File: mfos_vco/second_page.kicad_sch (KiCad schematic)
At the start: 0 parts

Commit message: Firs stages of second page
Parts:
- added C1, C2: 0.1uf, symbol Device:C_Polarized_Small_US
- added C14: 0.002uf, symbol Device:C_Polarized_Small_US
- added D2, D3: 1n4118, symbol Device:D_Small_Filled
- added R1, R6: 100k, symbol Device:R_Small_US
- added R12, R13, R25, R32: 10k, symbol Device:R_Small_US
- added R14, R21: 20K, symbol Device:R_Small_US
- added R20: 47k, symbol Device:R_Small_US
- added R22, R26: 1K, symbol Device:R_Small_US
- added R5, R7: 10k, symbol Device:R_Potentiometer_US
- added U4: TL074, symbol Amplifier_Operational:TL074
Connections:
- new net: R25.1, R32.1, U4.6 (-)
- new net: D3.2 (A), R26.1, R32.2, U4.7
- new net: R12.2, R20.1, U4.2 (-)
- new net: R5.3, R6.1
- new net: D2.2 (A), R20.2, R25.2, U4.1
- new net: C14.1, D2.1 (K), D3.1 (K), R13.1, R21.1
- new net: C1.1, R5.2, U4.3 (+)
- new net: C2.1, R7.2, U4.10 (+)
- new net: R1.1, R7.3
- new net: R14.2, R22.1, U4.8
- new net: R13.2, R14.1, U4.9 (-)
- new net: U4.13 (-), U4.14
- new net +12V: R1.2, R6.2
- new net -12V: C14.2, R21.2
- new net GND: C1.2, C2.2, R5.1, R7.1, U4.12 (+), U4.5 (+)
- new net RAW: R12.1
- new net RMP: R26.2
- new net TRI: R22.2

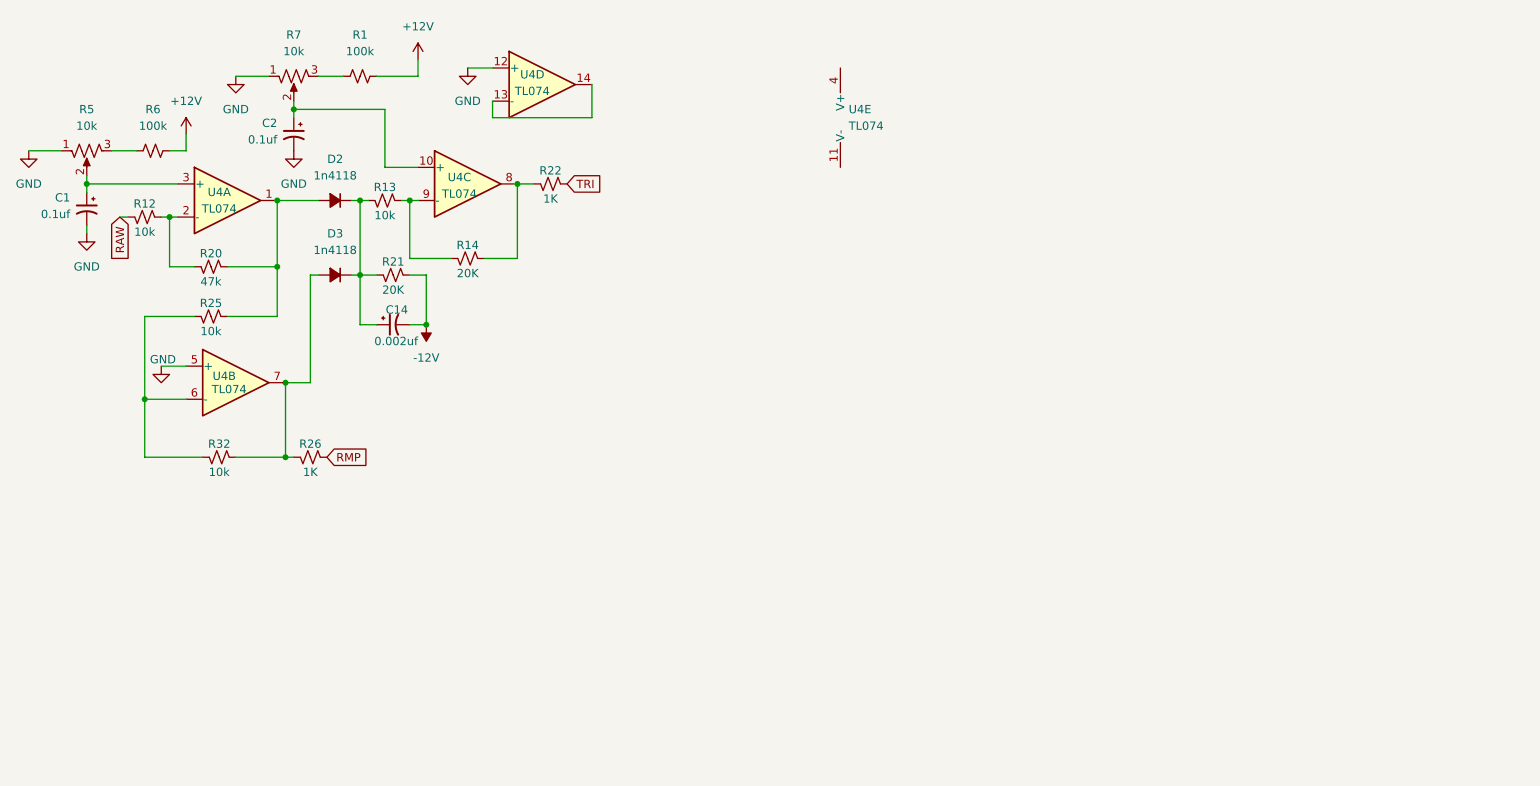
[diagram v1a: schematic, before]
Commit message: finished second page of schematic
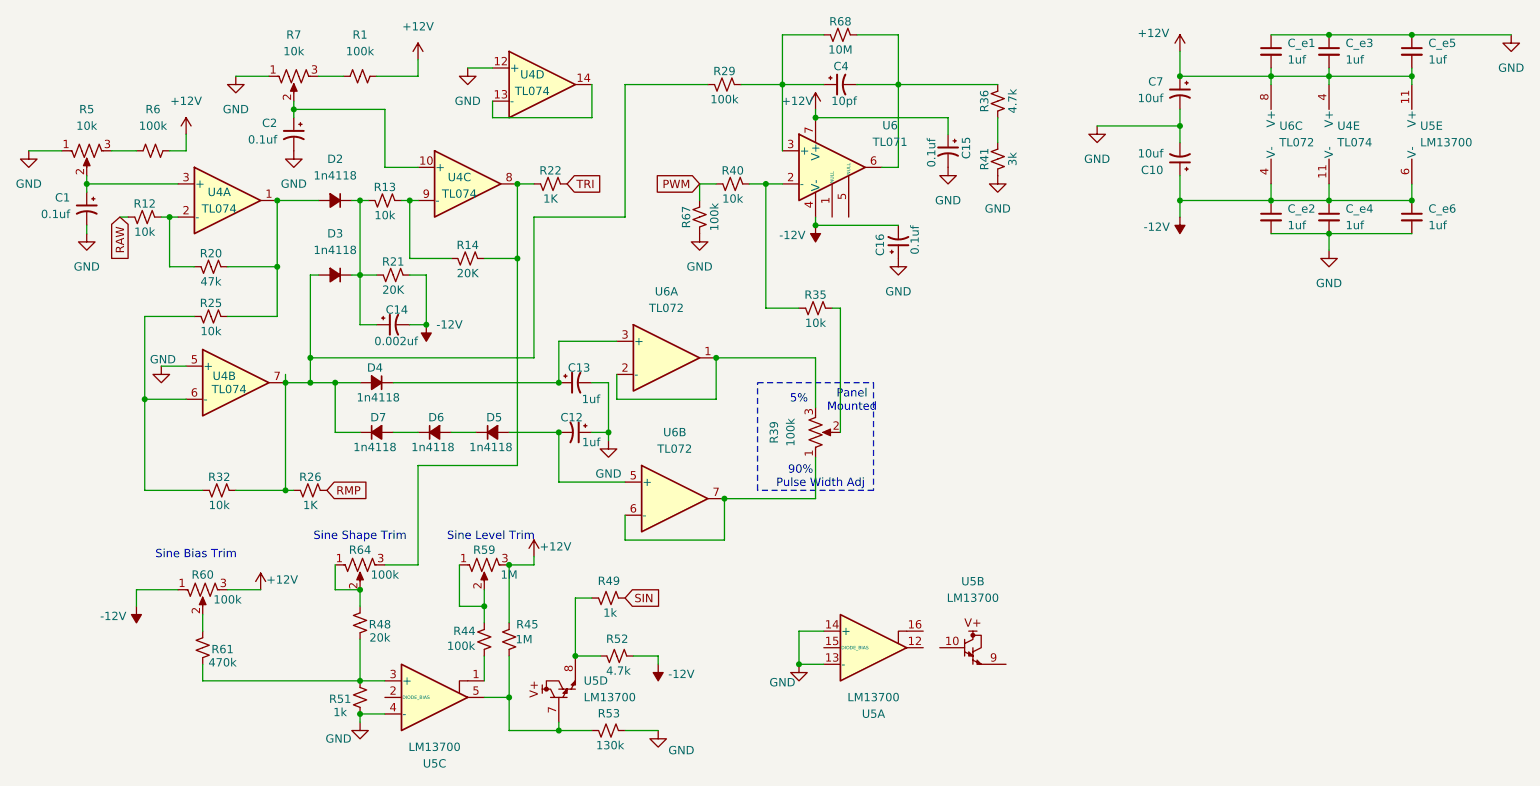
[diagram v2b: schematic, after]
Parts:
- added C10, C7: 10uf, symbol Device:C_Polarized_Small_US
- added C12, C13: 1uf, symbol Device:C_Polarized_Small_US
- added C15, C16: 0.1uf, symbol Device:C_Polarized_Small_US
- added C4: 10pf, symbol Device:C_Polarized_Small_US
- added C_e1, C_e2, C_e3, C_e4, C_e5, C_e6: 1uf, Capacitor_SMD:C_0805_2012Metric_Pad1.18x1.45mm_HandSolder, symbol Device:C_Small
- added D4, D5, D6, D7: 1n4118, symbol Device:D_Small_Filled
- added R29, R44, R67: 100k, symbol Device:R_Small_US
- added R35, R40: 10k, symbol Device:R_Small_US
- added R36, R52: 4.7k, symbol Device:R_Small_US
- added R39, R60, R64: 100k, symbol Device:R_Potentiometer_US
- added R41: 3k, symbol Device:R_Small_US
- added R45: 1M, symbol Device:R_Small_US
- added R48: 20k, symbol Device:R_Small_US
- added R49, R51: 1k, symbol Device:R_Small_US
- added R53: 130k, symbol Device:R_Small_US
- added R59: 1M, symbol Device:R_Potentiometer_US
- added R61: 470k, symbol Device:R_Small_US
- added R68: 10M, symbol Device:R_Small_US
- added U5: LM13700, symbol Amplifier_Operational:LM13700
- added U6: TL072, symbol Amplifier_Operational:TL072
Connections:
- net +12V: now also U4.4 (V+), C15.1, C7.1, C_e1.2, C_e3.2, C_e5.2, R45.2, R59.3, R60.3, U5.11 (V+), U6.7 (V+), U6.8 (V+)
- net -12V: now also U4.11 (V-), C10.1, C16.2, C_e2.1, C_e4.1, C_e6.1, R52.1, R60.1, U5.6 (V-), U6.4 (V-), U6.4 (V-)
- net GND: now also C10.2, C12.1, C13.2, C15.2, C16.1, C7.2, C_e1.1, C_e2.2, C_e3.1, C_e4.2, C_e5.1, C_e6.2, R41.1, R51.1, R53.1, R67.1, U5.13 (-), U5.14 (+), U5.4 (-)
- net at D3.2 (A), R26.1, R32.2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: now also D4.2 (A), D7.1 (K), R29.1
- net at R14.2, R22.1, U4.8: now also R64.3
- new net: C13.1, D4.1 (K), U6.3 (+)
- new net: R44.1, U5.1
- new net: R48.1, R51.2, R61.1, U5.3 (+)
- new net: R45.1, R53.2, U5.5, U5.7
- new net: R60.2, R61.2
- new net: R44.2, R59.1, R59.2
- new net: D5.1 (K), D6.2 (A)
- new net: C12.2, D5.2 (A), U6.5 (+)
- new net: R36.1, R41.2
- new net: C4.2, R36.2, R68.2, U6.6
- new net: R39.1, U6.6 (-), U6.7
- new net: R35.1, R40.2, U6.2 (-)
- new net: C4.1, R29.2, R68.1, U6.3 (+)
- new net: R49.2, R52.2, U5.8
- new net: R35.2, R39.2
- new net: R48.2, R64.1, R64.2
- new net: D6.1 (K), D7.2 (A)
- new net: R39.3, U6.1, U6.2 (-)
- new net PWM: R40.1, R67.2
- new net SIN: R49.1
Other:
- note added: "5%"
- note added: "90%"
- note added: "Panel Mounted"
- note added: "Pulse Width Adj"
- note added: "Sine Bias Trim"
- note added: "Sine Level Trim"
- note added: "Sine Shape Trim"
- moved on the sheet: R26, R32, U4E

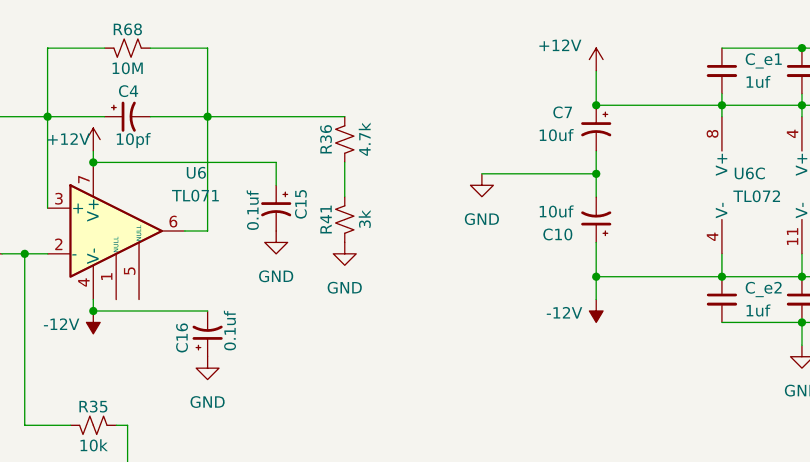
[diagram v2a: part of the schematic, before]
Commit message: Added output jumpers and custom foorprint
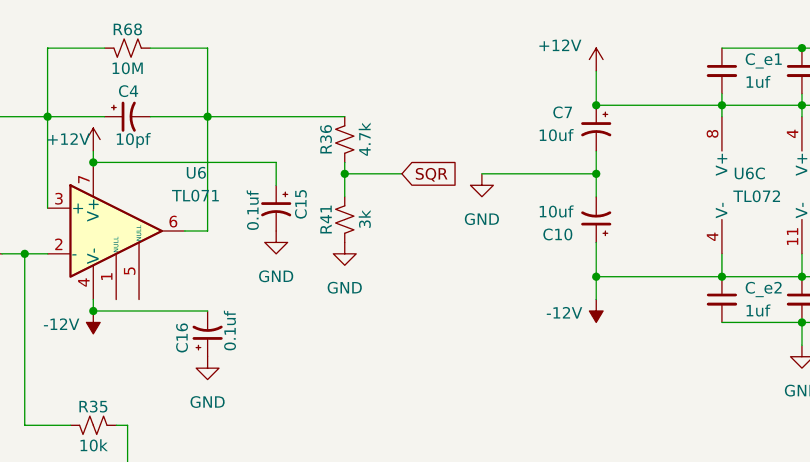
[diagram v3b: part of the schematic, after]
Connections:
- net SQR: now reaches R36.1, R41.2
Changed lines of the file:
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@@
+	)
+	(junction
+		(at 167.64 29.21)
+		(diameter 0)
+		(color 0 0 0 0)
 	)
 	(junction
@@
 	(wire
 		(pts
+			(xy 173.99 29.21) (xy 167.64 29.21)
+		)
+		(stroke
+			(width 0)
+			(type default)
+		)
+	)
+	(wire
+		(pts
 			(xy 139.7 64.77) (xy 139.7 72.39)
 		)
@@
 	(wire
 		(pts
-			(xy 167.64 27.94) (xy 167.64 31.75)
+			(xy 167.64 27.94) (xy 167.64 29.21)
 		)
 		(stroke
@@
 		(pts
 			(xy 78.74 96.52) (xy 73.66 96.52)
+		)
+		(stroke
+			(width 0)
+			(type default)
+		)
+	)
+	(wire
+		(pts
+			(xy 167.64 29.21) (xy 167.64 31.75)
 		)
 		(stroke
@@
 			(effects
 				(font
+					(size 1.27 1.27)
+				)
+				(justify left)
+				(hide yes)
+			)
+		)
+	)
+	(global_label "SQR"
+		(shape input)
+		(at 173.99 29.21 0)
+		(fields_autoplaced yes)
+		(effects
+			(font
+				(size 1.27 1.27)
+			)
+			(justify left)
+		)
+		(property "Intersheetrefs" "${INTERSHEET_REFS}"
+			(at 180.7852 29.21 0)
+			(effects
+				(font

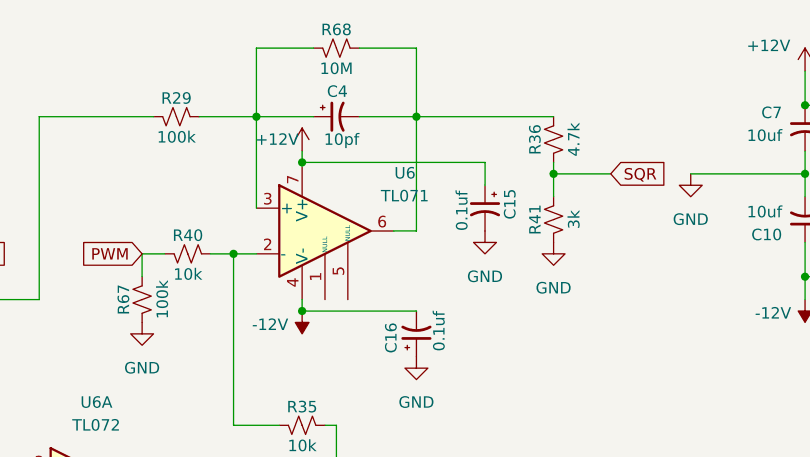
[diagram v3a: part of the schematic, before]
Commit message: added footprints
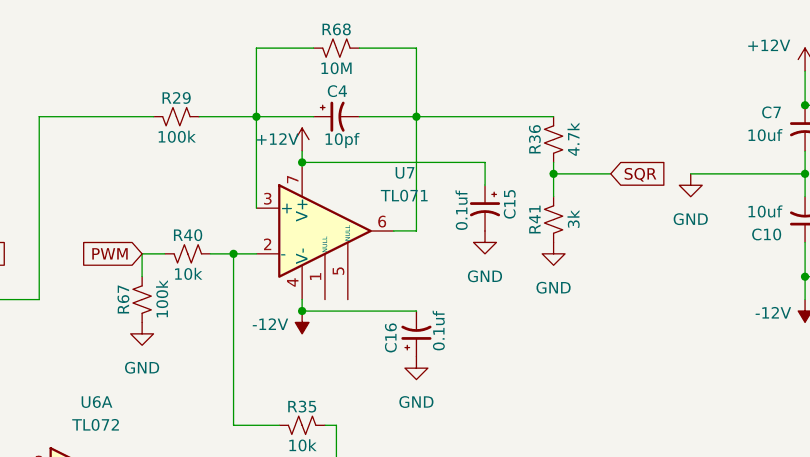
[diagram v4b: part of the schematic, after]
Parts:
- C1, C12, C13, C14, C15, C16, C2, C4: footprint (none) -> Capacitor_THT:CP_Radial_Tantal_D4.5mm_P5.00mm
- C10, C7: footprint (none) -> Capacitor_THT:CP_Radial_D5.0mm_P2.50mm
- D2, D3, D4, D5, D6, D7: footprint (none) -> Diode_THT:D_T-1_P5.08mm_Horizontal
- R1, R12, R13, R14, R20, R21, R22, R25, R26, R29, R32, R35, R36, R40, R41, R44, R45, R48, R49, R51, R52, R53, R6, R61, R67, R68: footprint (none) -> custom_footprints:R_SMD_AND_THT
- R5, R59, R60, R64, R7: footprint (none) -> Potentiometer_THT:Potentiometer_Bourns_3296W_Vertical
- U4: footprint (none) -> Package_DIP:DIP-14_W7.62mm
- U5: footprint (none) -> Package_DIP:DIP-16_W7.62mm
- U6: footprint (none) -> Package_DIP:DIP-8_W7.62mm
- U7: renamed from U6; footprint (none) -> Package_DIP:DIP-8_W7.62mm
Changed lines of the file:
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@@
 			)
 		)
-		(property "Footprint" ""
+		(property "Footprint" "Capacitor_THT:CP_Radial_Tantal_D4.5mm_P5.00mm"
 			(at 102.87 68.58 0)
 			(effects
@@
 			)
 		)
-		(property "Footprint" ""
+		(property "Footprint" "Package_DIP:DIP-16_W7.62mm"
 			(at 73.66 117.475 0)
 			(effects
@@
 			)
 		)
-		(property "Footprint" ""
+		(property "Footprint" "custom_footprints:R_SMD_AND_THT"
 			(at 92.71 107.95 0)
 			(effects
@@
 			)
 		)
-		(property "Footprint" ""
+		(property "Footprint" "Capacitor_THT:CP_Radial_Tantal_D4.5mm_P5.00mm"
 			(at 152.4 46.99 0)
 			(effects
@@
 			)
 		)
-		(property "Footprint" ""
+		(property "Footprint" "custom_footprints:R_SMD_AND_THT"
 			(at 45.72 109.22 0)
 			(effects
@@
 			)
 		)
-		(property "Footprint" ""
+		(property "Footprint" "Package_DIP:DIP-14_W7.62mm"
 			(at 49.53 66.04 0)
 			(effects
@@
 			)
 		)
-		(property "Footprint" ""
+		(property "Footprint" "custom_footprints:R_SMD_AND_THT"
 			(at 36.83 43.18 0)
 			(effects
@@
 			)
 		)
-		(property "Footprint" ""
+		(property "Footprint" "Capacitor_THT:CP_Radial_D5.0mm_P2.50mm"
 			(at 195.58 24.13 0)
 			(effects
@@
 			)
 		)
-		(property "Footprint" ""
+		(property "Footprint" "custom_footprints:R_SMD_AND_THT"
 			(at 38.1 33.02 0)
 			(effects
@@
 			)
 		)
-		(property "Footprint" ""
+		(property "Footprint" "custom_footprints:R_SMD_AND_THT"
 			(at 88.9 107.95 0)
 			(effects
@@
 			)
 		)
-		(property "Footprint" ""
+		(property "Footprint" "custom_footprints:R_SMD_AND_THT"
 			(at 46.99 58.42 0)
 			(effects
@@
 			)
 		)
-		(property "Footprint" ""
+		(property "Footprint" "Diode_THT:D_T-1_P5.08mm_Horizontal"
 			(at 66.04 52.07 90)
 			(effects
@@
 			)
 		)
-		(property "Footprint" ""
+		(property "Footprint" "custom_footprints:R_SMD_AND_THT"
 			(at 74.93 52.07 0)
 			(effects
@@
 			)
 		)
-		(property "Footprint" ""
+		(property "Footprint" "Diode_THT:D_T-1_P5.08mm_Horizontal"
 			(at 90.17 76.2 90)
 			(effects
@@
 			)
 		)
-		(property "Footprint" ""
+		(property "Footprint" "Capacitor_THT:CP_Radial_D5.0mm_P2.50mm"
 			(at 195.58 34.29 0)
 			(effects
@@
 			)
 		)
-		(property "Footprint" ""
+		(property "Footprint" "Capacitor_THT:CP_Radial_Tantal_D4.5mm_P5.00mm"
 			(at 102.87 76.2 0)
 			(effects
@@
 			)
 		)
-		(property "Footprint" ""
+		(property "Footprint" "Potentiometer_THT:Potentiometer_Bourns_3296W_Vertical"
 			(at 27.94 33.02 0)
 			(effects
@@
 			)
 		)
-		(property "Footprint" ""
+		(property "Footprint" "Diode_THT:D_T-1_P5.08mm_Horizontal"
 			(at 66.04 40.64 90)
 			(effects
@@
 			)
 		)
-		(property "Footprint" ""
+		(property "Footprint" "Package_DIP:DIP-14_W7.62mm"
 			(at 219.71 27.94 0)
 			(effects
@@
 			)
 		)
-		(property "Footprint" ""
+		(property "Footprint" "custom_footprints:R_SMD_AND_THT"
 			(at 167.64 25.4 0)
 			(effects
@@
 			)
 		)
-		(property "Footprint" ""
+		(property "Footprint" "Package_DIP:DIP-8_W7.62mm"
 			(at 118.11 86.36 0)
 			(effects
@@
 		(dnp no)
 		(fields_autoplaced yes)
-		(property "Reference" "U6"
+		(property "Reference" "U7"
 			(at 151.13 29.1398 0)
 			(effects
@@
 			)
 		)
-		(property "Footprint" ""
+		(property "Footprint" "Package_DIP:DIP-8_W7.62mm"
 			(at 143.51 34.29 0)
 			(effects
@@
 			(project ""
 				(path "/db27d43e-bcf4-48a8-8785-18123cee165a/ea17d4b3-540b-4353-b4a9-31ae80237135"
-					(reference "U6")
+					(reference "U7")
 					(unit 1)
 				)
@@
 			)
 		)
-		(property "Footprint" ""
+		(property "Footprint" "custom_footprints:R_SMD_AND_THT"
 			(at 143.51 15.24 0)
 			(effects
@@
 			)
 		)
-		(property "Footprint" ""
+		(property "Footprint" "Package_DIP:DIP-16_W7.62mm"
 			(at 158.75 108.585 0)
 			(effects
@@
 			)
 		)
-		(property "Footprint" ""
+		(property "Footprint" "Potentiometer_THT:Potentiometer_Bourns_3296W_Vertical"
 			(at 59.69 21.59 0)
 			(effects
@@
 			)
 		)
-		(property "Footprint" ""
+		(property "Footprint" "Capacitor_THT:CP_Radial_Tantal_D4.5mm_P5.00mm"
 			(at 74.93 59.69 0)
 			(effects
@@
 			)
 		)
-		(property "Footprint" ""
+		(property "Footprint" "Package_DIP:DIP-16_W7.62mm"
 			(at 99.695 120.65 0)
 			(effects
@@
 			)
 		)
-		(property "Footprint" ""
+		(property "Footprint" "custom_footprints:R_SMD_AND_THT"
 			(at 48.26 85.09 0)
 			(effects
@@
 			)
 		)
-		(property "Footprint" ""
+		(property "Footprint" "Capacitor_THT:CP_Radial_Tantal_D4.5mm_P5.00mm"
 			(at 143.51 22.86 0)
 			(effects
@@
 			)
 		)
-		(property "Footprint" ""
+		(property "Footprint" "custom_footprints:R_SMD_AND_THT"
 			(at 62.23 85.09 0)
 			(effects
@@
 			)
 		)
-		(property "Footprint" ""
+		(property "Footprint" "custom_footprints:R_SMD_AND_THT"
 			(at 99.06 38.1 0)
 			(effects
@@
 			)
 		)
-		(property "Footprint" ""
+		(property "Footprint" "Potentiometer_THT:Potentiometer_Bourns_3296W_Vertical"
 			(at 88.9 96.52 0)
 			(effects
@@
 			)
 		)
-		(property "Footprint" ""
+		(property "Footprint" "custom_footprints:R_SMD_AND_THT"
 			(at 107.95 121.92 0)
 			(effects
@@
 			)
 		)
-		(property "Footprint" ""
+		(property "Footprint" "Package_DIP:DIP-14_W7.62mm"
 			(at 85.09 35.56 0)
 			(effects
@@
 			)
 		)
-		(property "Footprint" ""
+		(property "Footprint" "custom_footprints:R_SMD_AND_THT"
 			(at 86.36 49.53 0)
 			(effects
@@
 			)
 		)
-		(property "Footprint" ""
+		(property "Footprint" "custom_footprints:R_SMD_AND_THT"
 			(at 125.73 22.86 0)
 			(effects
@@
 			)
 		)
-		(property "Footprint" ""
+		(property "Footprint" "custom_footprints:R_SMD_AND_THT"
 			(at 46.99 50.8 0)
 			(effects
@@
 			)
 		)
-		(property "Footprint" ""
+		(property "Footprint" "custom_footprints:R_SMD_AND_THT"
 			(at 167.64 34.29 0)
 			(effects
@@
 			)
 		)
-		(property "Footprint" ""
+		(property "Footprint" "Capacitor_THT:CP_Radial_Tantal_D4.5mm_P5.00mm"
 			(at 27.94 41.91 0)
 			(effects
@@
 			)
 		)
-		(property "Footprint" ""
+		(property "Footprint" "custom_footprints:R_SMD_AND_THT"
 			(at 107.95 101.6 0)
 			(effects
@@
 			)
 		)
-		(property "Footprint" ""
+		(property "Footprint" "custom_footprints:R_SMD_AND_THT"
 			(at 69.85 21.59 0)
 			(effects
@@
 			)
 		)
-		(property "Footprint" ""
+		(property "Footprint" "Package_DIP:DIP-14_W7.62mm"
 			(at 48.26 38.1 0)
 			(effects
@@
 			)
 		)
-		(property "Footprint" ""
+		(property "Footprint" "Capacitor_THT:CP_Radial_Tantal_D4.5mm_P5.00mm"
 			(at 59.69 30.48 0)
 			(effects
@@
 			)
 		)
-		(property "Footprint" ""
+		(property "Footprint" "Package_DIP:DIP-16_W7.62mm"
 			(at 140.97 109.855 0)
 			(effects
@@
 			)
 		)
-		(property "Footprint" ""
+		(property "Footprint" "Package_DIP:DIP-16_W7.62mm"
 			(at 226.06 29.845 0)
 			(effects
@@
 			)
 		)
-		(property "Footprint" ""
+		(property "Footprint" "custom_footprints:R_SMD_AND_THT"
 			(at 139.7 57.15 0)
 			(effects
@@
 			)
 		)
-		(property "Footprint" ""
+		(property "Footprint" "Potentiometer_THT:Potentiometer_Bourns_3296W_Vertical"
 			(at 69.85 96.52 0)
 			(effects
@@
 			)
 		)
-		(property "Footprint" ""
+		(property "Footprint" "custom_footprints:R_SMD_AND_THT"
 			(at 69.85 105.41 0)
 			(effects
@@
 			)
 		)
-		(property "Footprint" ""
+		(property "Footprint" "custom_footprints:R_SMD_AND_THT"
 			(at 73.66 40.64 0)
 			(effects
@@
 			)
 		)
-		(property "Footprint" ""
+		(property "Footprint" "Diode_THT:D_T-1_P5.08mm_Horizontal"
 			(at 72.39 68.58 90)
 			(effects
@@
 			)
 		)
-		(property "Footprint" ""
+		(property "Footprint" "Capacitor_THT:CP_Radial_Tantal_D4.5mm_P5.00mm"
 			(at 160.02 33.02 0)
 			(effects
@@
 			)
 		)
-		(property "Footprint" ""
+		(property "Footprint" "Diode_THT:D_T-1_P5.08mm_Horizontal"
 			(at 81.28 76.2 90)
 			(effects
@@
 			)
 		)
-		(property "Footprint" ""
+		(property "Footprint" "custom_footprints:R_SMD_AND_THT"
 			(at 109.22 110.49 0)
 			(effects
@@
 			)
 		)
-		(property "Footprint" ""
+		(property "Footprint" "Potentiometer_THT:Potentiometer_Bourns_3296W_Vertical"
 			(at 45.72 100.33 0)
 			(effects
@@
 			)
 		)
-		(property "Footprint" ""
+		(property "Footprint" "Package_DIP:DIP-8_W7.62mm"
 			(at 116.84 64.77 0)
 			(effects
@@
 			)
 		)
-		(property "Footprint" ""
+		(property "Footprint" "Package_DIP:DIP-14_W7.62mm"
 			(at 96.52 20.32 0)
 			(effects
@@
 			)
 		)
-		(property "Footprint" ""
+		(property "Footprint" "Diode_THT:D_T-1_P5.08mm_Horizontal"
 			(at 72.39 76.2 90)
 			(effects
@@
 			)
 		)
-		(property "Footprint" ""
+		(property "Footprint" "custom_footprints:R_SMD_AND_THT"
 			(at 127 38.1 0)
 			(effects
@@
 			)
 		)
-		(property "Footprint" ""
+		(property "Footprint" "custom_footprints:R_SMD_AND_THT"
 			(at 121.92 43.18 0)
 			(effects
@@
 			)
 		)
-		(property "Footprint" ""
+		(property "Footprint" "custom_footprints:R_SMD_AND_THT"
 			(at 69.85 116.84 0)
 			(effects
@@
 			)
 		)
-		(property "Footprint" ""
+		(property "Footprint" "Package_DIP:DIP-8_W7.62mm"
 			(at 212.09 30.48 0)
 			(effects
